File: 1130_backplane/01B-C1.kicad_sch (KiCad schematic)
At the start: 86 parts

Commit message: DN101-DN111 added to backplane schematics, DN111 01B-A1 connections made, 01B-B1 connections to be made when all signals on connectors
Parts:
- removed J431, J432, J433, J434, J435, J436, J437, J438, J439, J440, J441, J442, J443, J444, J445, J446, J447, J448, J449, J450, J451, J452, J453, J454, J455, J456, J457, J458, J459, J460, J461, J462, J463, J464, J465, J466, J467, J468, J469, J470, J471, J472, J473, J474, J475, J476, J477, J478, J479, J480, J481, J482, J483, J484, J485, J486, J487, J488, J489, J490, J491, J492, J493, J494, J495, J496, J497, J498, J499, J500, J501, J502, J503, J504, J505, J506, J507, J508, J509, J510, J511, J512, J513, J514, J515, J516: ~, symbol Connector_Generic:Conn_02x12_Row_Letter_First
- added J? (x86): ~, symbol Connector_Generic:Conn_02x12_Row_Letter_First
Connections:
- net +3V: now also J?.b2 (Pin_b2), J?.b2 (Pin_b2), J?.b2 (Pin_b2), J?.b2 (Pin_b2), J?.b2 (Pin_b2), J?.b2 (Pin_b2), J?.b2 (Pin_b2), J?.b2 (Pin_b2), J?.b2 (Pin_b2), J?.b2 (Pin_b2), J?.b2 (Pin_b2), J?.b2 (Pin_b2), J?.b2 (Pin_b2), J?.b2 (Pin_b2), J?.b2 (Pin_b2), J?.b2 (Pin_b2), J?.b2 (Pin_b2), J?.b2 (Pin_b2), J?.b2 (Pin_b2), J?.b2 (Pin_b2), J?.b2 (Pin_b2), J?.b2 (Pin_b2), J?.b2 (Pin_b2), J?.b2 (Pin_b2), J?.b2 (Pin_b2), J?.b2 (Pin_b2), J?.b2 (Pin_b2), J?.b2 (Pin_b2), J?.b2 (Pin_b2), J?.b2 (Pin_b2), J?.b2 (Pin_b2), J?.b2 (Pin_b2), J?.b2 (Pin_b2), J?.b2 (Pin_b2), J?.b2 (Pin_b2), J?.b2 (Pin_b2), J?.b2 (Pin_b2), J?.b2 (Pin_b2), J?.b2 (Pin_b2), J?.b2 (Pin_b2), J?.b2 (Pin_b2), J?.b2 (Pin_b2), J?.b2 (Pin_b2), J?.b2 (Pin_b2), J?.b2 (Pin_b2), J?.b2 (Pin_b2), J?.b2 (Pin_b2), J?.b2 (Pin_b2), J?.b2 (Pin_b2), J?.b2 (Pin_b2), J?.b2 (Pin_b2), J?.b2 (Pin_b2), J?.b2 (Pin_b2), J?.b2 (Pin_b2), J?.b2 (Pin_b2), J?.b2 (Pin_b2), J?.b2 (Pin_b2), J?.b2 (Pin_b2), J?.b2 (Pin_b2), J?.b2 (Pin_b2), J?.b2 (Pin_b2), J?.b2 (Pin_b2), J?.b2 (Pin_b2), J?.b2 (Pin_b2), J?.b2 (Pin_b2), J?.b2 (Pin_b2), J?.b2 (Pin_b2), J?.b2 (Pin_b2), J?.b2 (Pin_b2), J?.b2 (Pin_b2), J?.b2 (Pin_b2), J?.b2 (Pin_b2), J?.b2 (Pin_b2), J?.b2 (Pin_b2), J?.b2 (Pin_b2), J?.b2 (Pin_b2), J?.b2 (Pin_b2), J?.b2 (Pin_b2)
- net +6V: now also J?.a10 (Pin_a10), J?.a10 (Pin_a10), J?.a10 (Pin_a10), J?.a10 (Pin_a10), J?.a10 (Pin_a10), J?.a10 (Pin_a10), J?.a10 (Pin_a10), J?.a10 (Pin_a10), J?.a10 (Pin_a10), J?.a10 (Pin_a10), J?.a10 (Pin_a10), J?.a10 (Pin_a10), J?.a10 (Pin_a10), J?.a10 (Pin_a10), J?.a10 (Pin_a10), J?.a10 (Pin_a10), J?.a10 (Pin_a10), J?.a10 (Pin_a10), J?.a10 (Pin_a10), J?.a10 (Pin_a10), J?.a10 (Pin_a10), J?.a10 (Pin_a10), J?.a10 (Pin_a10), J?.a10 (Pin_a10), J?.a10 (Pin_a10), J?.a10 (Pin_a10), J?.a10 (Pin_a10), J?.a10 (Pin_a10), J?.a10 (Pin_a10), J?.a10 (Pin_a10), J?.a10 (Pin_a10), J?.a10 (Pin_a10), J?.a10 (Pin_a10), J?.a10 (Pin_a10), J?.a10 (Pin_a10), J?.a10 (Pin_a10), J?.a10 (Pin_a10), J?.a10 (Pin_a10), J?.a10 (Pin_a10), J?.a10 (Pin_a10), J?.a10 (Pin_a10), J?.a10 (Pin_a10), J?.a10 (Pin_a10), J?.a10 (Pin_a10), J?.a10 (Pin_a10), J?.a10 (Pin_a10), J?.a10 (Pin_a10), J?.a10 (Pin_a10), J?.a10 (Pin_a10), J?.a10 (Pin_a10), J?.a10 (Pin_a10), J?.a10 (Pin_a10), J?.a10 (Pin_a10), J?.a10 (Pin_a10), J?.a10 (Pin_a10), J?.a10 (Pin_a10), J?.a10 (Pin_a10), J?.a10 (Pin_a10), J?.a10 (Pin_a10), J?.a10 (Pin_a10), J?.a10 (Pin_a10), J?.a10 (Pin_a10), J?.a10 (Pin_a10), J?.a10 (Pin_a10), J?.a10 (Pin_a10), J?.a10 (Pin_a10), J?.a10 (Pin_a10), J?.a10 (Pin_a10), J?.a10 (Pin_a10), J?.a10 (Pin_a10), J?.a10 (Pin_a10), J?.a10 (Pin_a10), J?.a10 (Pin_a10), J?.a10 (Pin_a10), J?.a10 (Pin_a10), J?.a10 (Pin_a10), J?.a10 (Pin_a10), J?.a10 (Pin_a10)
- net -3V: now also J?.a5 (Pin_a5), J?.a5 (Pin_a5), J?.a5 (Pin_a5), J?.a5 (Pin_a5), J?.a5 (Pin_a5), J?.a5 (Pin_a5), J?.a5 (Pin_a5), J?.a5 (Pin_a5), J?.a5 (Pin_a5), J?.a5 (Pin_a5), J?.a5 (Pin_a5), J?.a5 (Pin_a5), J?.a5 (Pin_a5), J?.a5 (Pin_a5), J?.a5 (Pin_a5), J?.a5 (Pin_a5), J?.a5 (Pin_a5), J?.a5 (Pin_a5), J?.a5 (Pin_a5), J?.a5 (Pin_a5), J?.a5 (Pin_a5), J?.a5 (Pin_a5), J?.a5 (Pin_a5), J?.a5 (Pin_a5), J?.a5 (Pin_a5), J?.a5 (Pin_a5), J?.a5 (Pin_a5), J?.a5 (Pin_a5), J?.a5 (Pin_a5), J?.a5 (Pin_a5), J?.a5 (Pin_a5), J?.a5 (Pin_a5), J?.a5 (Pin_a5), J?.a5 (Pin_a5), J?.a5 (Pin_a5), J?.a5 (Pin_a5), J?.a5 (Pin_a5), J?.a5 (Pin_a5), J?.a5 (Pin_a5), J?.a5 (Pin_a5), J?.a5 (Pin_a5), J?.a5 (Pin_a5), J?.a5 (Pin_a5), J?.a5 (Pin_a5), J?.a5 (Pin_a5), J?.a5 (Pin_a5), J?.a5 (Pin_a5), J?.a5 (Pin_a5), J?.a5 (Pin_a5), J?.a5 (Pin_a5), J?.a5 (Pin_a5), J?.a5 (Pin_a5), J?.a5 (Pin_a5), J?.a5 (Pin_a5), J?.a5 (Pin_a5), J?.a5 (Pin_a5), J?.a5 (Pin_a5), J?.a5 (Pin_a5), J?.a5 (Pin_a5), J?.a5 (Pin_a5), J?.a5 (Pin_a5), J?.a5 (Pin_a5), J?.a5 (Pin_a5), J?.a5 (Pin_a5), J?.a5 (Pin_a5), J?.a5 (Pin_a5), J?.a5 (Pin_a5), J?.a5 (Pin_a5), J?.a5 (Pin_a5), J?.a5 (Pin_a5), J?.a5 (Pin_a5), J?.a5 (Pin_a5), J?.a5 (Pin_a5), J?.a5 (Pin_a5), J?.a5 (Pin_a5), J?.a5 (Pin_a5), J?.a5 (Pin_a5), J?.a5 (Pin_a5)
- net GND: now also J?.b7 (Pin_b7), J?.b7 (Pin_b7), J?.b7 (Pin_b7), J?.b7 (Pin_b7), J?.b7 (Pin_b7), J?.b7 (Pin_b7), J?.b7 (Pin_b7), J?.b7 (Pin_b7), J?.b7 (Pin_b7), J?.b7 (Pin_b7), J?.b7 (Pin_b7), J?.b7 (Pin_b7), J?.b7 (Pin_b7), J?.b7 (Pin_b7), J?.b7 (Pin_b7), J?.b7 (Pin_b7), J?.b7 (Pin_b7), J?.b7 (Pin_b7), J?.b7 (Pin_b7), J?.b7 (Pin_b7), J?.b7 (Pin_b7), J?.b7 (Pin_b7), J?.b7 (Pin_b7), J?.b7 (Pin_b7), J?.b7 (Pin_b7), J?.b7 (Pin_b7), J?.b7 (Pin_b7), J?.b7 (Pin_b7), J?.b7 (Pin_b7), J?.b7 (Pin_b7), J?.b7 (Pin_b7), J?.b7 (Pin_b7), J?.b7 (Pin_b7), J?.b7 (Pin_b7), J?.b7 (Pin_b7), J?.b7 (Pin_b7), J?.b7 (Pin_b7), J?.b7 (Pin_b7), J?.b7 (Pin_b7), J?.b7 (Pin_b7), J?.b7 (Pin_b7), J?.b7 (Pin_b7), J?.b7 (Pin_b7), J?.b7 (Pin_b7), J?.b7 (Pin_b7), J?.b7 (Pin_b7), J?.b7 (Pin_b7), J?.b7 (Pin_b7), J?.b7 (Pin_b7), J?.b7 (Pin_b7), J?.b7 (Pin_b7), J?.b7 (Pin_b7), J?.b7 (Pin_b7), J?.b7 (Pin_b7), J?.b7 (Pin_b7), J?.b7 (Pin_b7), J?.b7 (Pin_b7), J?.b7 (Pin_b7), J?.b7 (Pin_b7), J?.b7 (Pin_b7), J?.b7 (Pin_b7), J?.b7 (Pin_b7), J?.b7 (Pin_b7), J?.b7 (Pin_b7), J?.b7 (Pin_b7), J?.b7 (Pin_b7), J?.b7 (Pin_b7), J?.b7 (Pin_b7), J?.b7 (Pin_b7), J?.b7 (Pin_b7), J?.b7 (Pin_b7), J?.b7 (Pin_b7), J?.b7 (Pin_b7), J?.b7 (Pin_b7), J?.b7 (Pin_b7), J?.b7 (Pin_b7), J?.b7 (Pin_b7), J?.b7 (Pin_b7), J?.b7 (Pin_b7), J?.b7 (Pin_b7), J?.b7 (Pin_b7), J?.b7 (Pin_b7), J?.b7 (Pin_b7), J?.b7 (Pin_b7), J?.b7 (Pin_b7), J?.b7 (Pin_b7)

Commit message: Add labels for bottom T[x] connectors, finished page DU101.
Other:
- moved on the sheet: J?

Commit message: Redo annotations...
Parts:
- gave numbers to parts that had none: 86

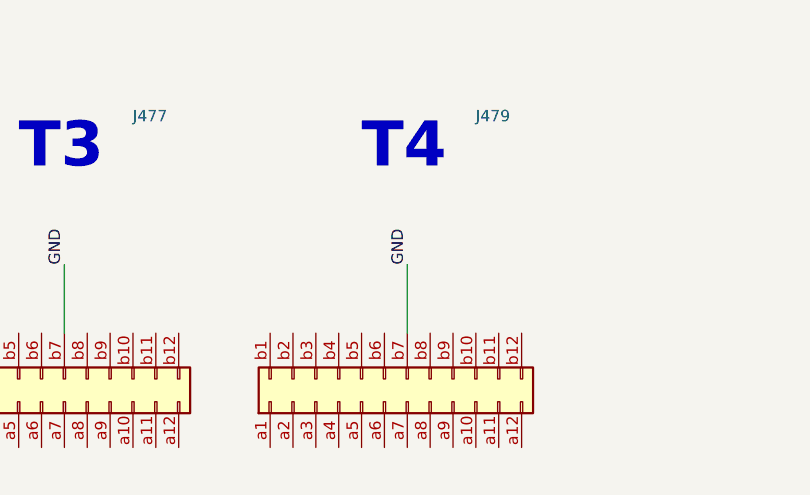
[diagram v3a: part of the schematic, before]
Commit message: Finish page KR101-KR111
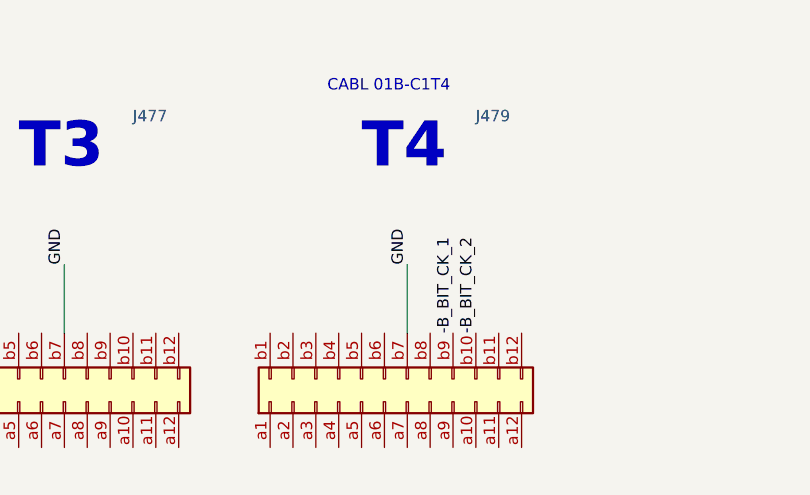
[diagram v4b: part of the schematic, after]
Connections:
- net -B_BIT_CK_2: now reaches J479.b10 (Pin_b10)
- net -B_BIT_CK_1: now reaches J479.b9 (Pin_b9)
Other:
- note added: "CABL 01B-C1T4"
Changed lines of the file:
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@@
     (effects (font (size 5 5) (thickness 1) bold) (justify left bottom))
+  )
+  (text "CABL 01B-C1T4" (at 469.9 24.13 0)
+    (effects (font (size 1.27 1.27)) (justify left bottom))
   )
   (text "C" (at 163.83 337.82 0)
@@
     (effects (font (size 1.27 1.27)) (justify right bottom))
   )
+  (label "-B_BIT_CK_1" (at 483.87 50.8 90)
+    (effects (font (size 1.27 1.27)) (justify left bottom))
+  )
   (label "-3V" (at 469.9 266.7 180)
     (effects (font (size 1.27 1.27)) (justify right bottom))
@@
     (effects (font (size 1.27 1.27)) (justify left bottom))
   )
+  (label "-B_BIT_CK_2" (at 486.41 50.8 90)
+    (effects (font (size 1.27 1.27)) (justify left bottom))
+  )

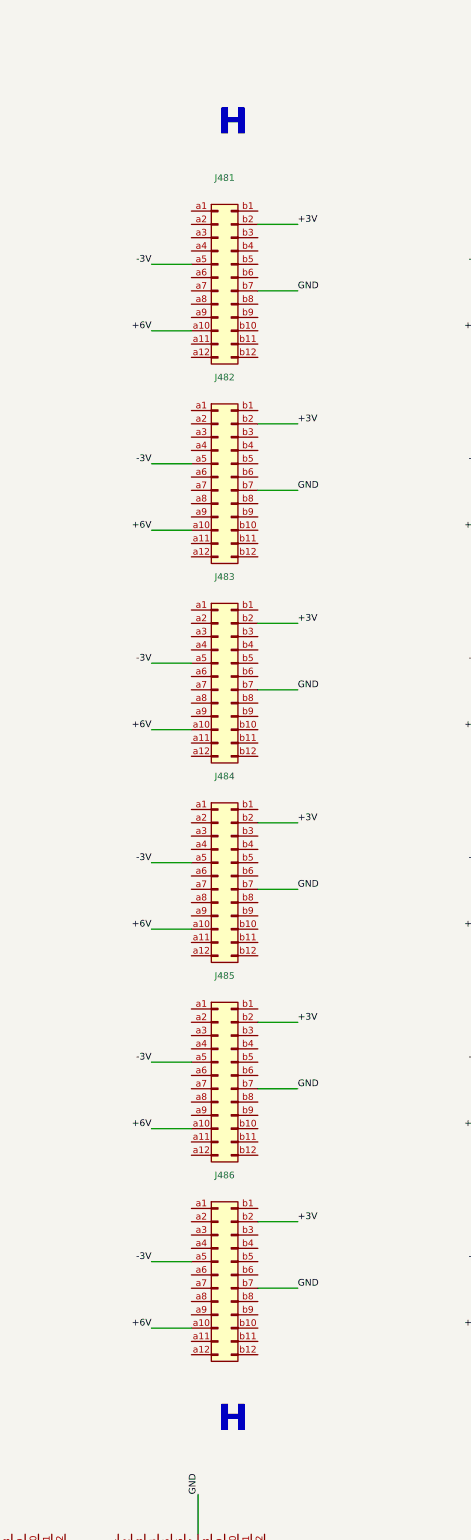
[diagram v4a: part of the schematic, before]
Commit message: Finish page KU301-KU311, minor column label fix.
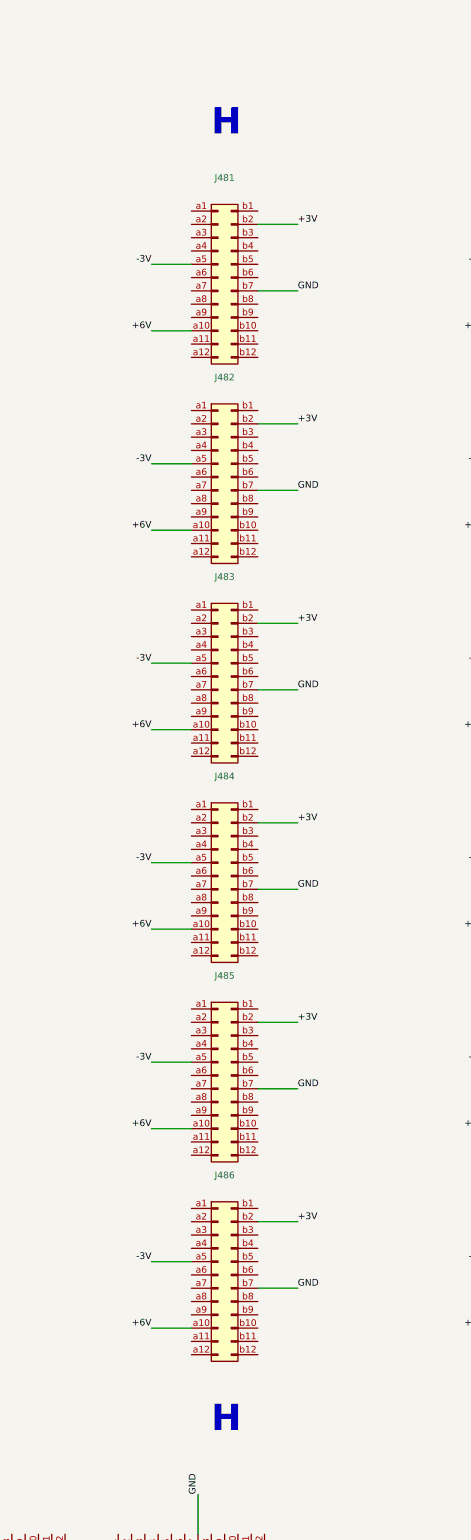
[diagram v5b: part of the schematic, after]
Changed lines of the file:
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@@
     (effects (font (size 5 5) (thickness 1) bold) (justify left bottom))
   )
-  (text "H" (at 482.6 337.82 0)
+  (text "H" (at 481.33 337.82 0)
     (effects (font (size 5 5) (thickness 1) bold) (justify left bottom))
   )
@@
     (effects (font (size 1.27 1.27)) (justify left bottom))
   )
-  (text "H" (at 482.6 90.17 0)
+  (text "H" (at 481.33 90.17 0)
     (effects (font (size 5 5) (thickness 1) bold) (justify left bottom))
   )

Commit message: Actually finish MB101...
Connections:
- net -STORAGE_ADDRESS_10: now reaches J477.a10 (Pin_a10)
- net -STORAGE_ADDRESS_10: now also J477.a7 (Pin_a7)
- net -STORAGE_ADDRESS_12: now reaches J477.a11 (Pin_a11)
- net -STORAGE_ADDRESS_14: now reaches J477.a12 (Pin_a12)
- net -STORAGE_ADDRESS_4: now reaches J477.a3 (Pin_a3)
- net -STORAGE_ADDRESS_6: now reaches J477.a4 (Pin_a4)
- net -STORAGE_ADDRESS_8: now reaches J477.a9 (Pin_a9)
- net -STORAGE_ADDRESS_11: now reaches J477.b10 (Pin_b10)
- net -STORAGE_ADDRESS_13: now reaches J477.b11 (Pin_b11)
- net -STORAGE_ADDRESS_15: now reaches J477.b12 (Pin_b12)
- net -STORAGE_ADDRESS_3: now reaches J477.b2 (Pin_b2)
- net -STORAGE_ADDRESS_5: now reaches J477.b3 (Pin_b3)
- net -STORAGE_ADDRESS_7: now reaches J477.b4 (Pin_b4)
- net -STORAGE_ADDRESS_9: now reaches J477.b9 (Pin_b9)
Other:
- note added: "CABL 01B-B1T3"
- note added: "CABL 01B-B1T4"
- note removed: "CABL 01B-C1T4"
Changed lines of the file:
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@@
     (effects (font (size 5 5) (thickness 1) bold) (justify left bottom))
   )
-  (text "CABL 01B-C1T4" (at 469.9 24.13 0)
+  (text "CABL 01B-B1T4" (at 469.9 24.13 0)
     (effects (font (size 1.27 1.27)) (justify left bottom))
   )
@@
     (effects (font (size 1.27 1.27)) (justify left bottom))
   )
+  (text "CABL 01B-B1T3" (at 431.8 24.13 0)
+    (effects (font (size 1.27 1.27)) (justify left bottom))
+  )
   (text "A" (at 29.21 38.1 0)
     (effects (font (size 5 5) (thickness 1) bold) (justify left bottom))
@@
     (effects (font (size 1.27 1.27)) (justify left bottom))
   )
+  (label "-STORAGE_ADDRESS_3" (at 427.99 50.8 90)
+    (effects (font (size 1.27 1.27)) (justify left bottom))
+  )
   (label "+3V" (at 497.84 259.08 0)
     (effects (font (size 1.27 1.27)) (justify left bottom))
@@
     (effects (font (size 1.27 1.27)) (justify right bottom))
   )
+  (label "-STORAGE_ADDRESS_13" (at 450.85 50.8 90)
+    (effects (font (size 1.27 1.27)) (justify left bottom))
+  )
   (label "GND" (at 116.84 233.68 0)
     (effects (font (size 1.27 1.27)) (justify left bottom))
@@
     (effects (font (size 1.27 1.27)) (justify right bottom))
   )
+  (label "-STORAGE_ADDRESS_9" (at 445.77 50.8 90)
+    (effects (font (size 1.27 1.27)) (justify left bottom))
+  )
   (label "GND" (at 624.84 119.38 0)
     (effects (font (size 1.27 1.27)) (justify left bottom))
@@
     (effects (font (size 1.27 1.27)) (justify left bottom))
   )
+  (label "-STORAGE_ADDRESS_11" (at 448.31 50.8 90)
+    (effects (font (size 1.27 1.27)) (justify left bottom))
+  )
   (label "GND" (at 624.84 309.88 0)
     (effects (font (size 1.27 1.27)) (justify left bottom))
@@
     (effects (font (size 1.27 1.27)) (justify left bottom))
   )
+  (label "-STORAGE_ADDRESS_6" (at 433.07 63.5 270)
+    (effects (font (size 1.27 1.27)) (justify right bottom))
+  )
   (label "+6V" (at 152.4 165.1 180)
     (effects (font (size 1.27 1.27)) (justify right bottom))
@@
     (effects (font (size 1.27 1.27)) (justify right bottom))
   )
+  (label "-STORAGE_ADDRESS_4" (at 430.53 63.5 270)
+    (effects (font (size 1.27 1.27)) (justify right bottom))
+  )
   (label "-3V" (at 25.4 304.8 180)
     (effects (font (size 1.27 1.27)) (justify right bottom))
@@
     (effects (font (size 1.27 1.27)) (justify left bottom))
   )
+  (label "-STORAGE_ADDRESS_10" (at 448.31 63.5 270)
+    (effects (font (size 1.27 1.27)) (justify right bottom))
+  )
   (label "GND" (at 497.84 119.38 0)
     (effects (font (size 1.27 1.27)) (justify left bottom))
@@
     (effects (font (size 1.27 1.27)) (justify left bottom))
   )
+  (label "-STORAGE_ADDRESS_10" (at 440.69 63.5 270)
+    (effects (font (size 1.27 1.27)) (justify right bottom))
+  )
   (label "-3V" (at 406.4 152.4 180)
     (effects (font (size 1.27 1.27)) (justify right bottom))
@@
     (effects (font (size 1.27 1.27)) (justify right bottom))
   )
+  (label "-STORAGE_ADDRESS_14" (at 453.39 63.5 270)
+    (effects (font (size 1.27 1.27)) (justify right bottom))
+  )
   (label "+3V" (at 624.84 182.88 0)
     (effects (font (size 1.27 1.27)) (justify left bottom))
@@
     (effects (font (size 1.27 1.27)) (justify right bottom))
   )
+  (label "-STORAGE_ADDRESS_7" (at 433.07 50.8 90)
+    (effects (font (size 1.27 1.27)) (justify left bottom))
+  )
   (label "GND" (at 243.84 195.58 0)
     (effects (font (size 1.27 1.27)) (justify left bottom))
@@
     (effects (font (size 1.27 1.27)) (justify left bottom))
   )
+  (label "-STORAGE_ADDRESS_15" (at 453.39 50.8 90)
+    (effects (font (size 1.27 1.27)) (justify left bottom))
+  )
   (label "+3V" (at 561.34 259.08 0)
     (effects (font (size 1.27 1.27)) (justify left bottom))
@@
     (effects (font (size 1.27 1.27)) (justify right bottom))
   )
+  (label "-STORAGE_ADDRESS_5" (at 430.53 50.8 90)
+    (effects (font (size 1.27 1.27)) (justify left bottom))
+  )
   (label "+6V" (at 25.4 279.4 180)
     (effects (font (size 1.27 1.27)) (justify right bottom))
@@
     (effects (font (size 1.27 1.27)) (justify left bottom))
   )
+  (label "-STORAGE_ADDRESS_12" (at 450.85 63.5 270)
+    (effects (font (size 1.27 1.27)) (justify right bottom))
+  )
   (label "GND" (at 624.84 157.48 0)
     (effects (font (size 1.27 1.27)) (justify left bottom))
@@
     (effects (font (size 1.27 1.27)) (justify left bottom))
   )
+  (label "-STORAGE_ADDRESS_8" (at 445.77 63.5 270)
+    (effects (font (size 1.27 1.27)) (justify right bottom))
+  )
   (label "+6V" (at 406.4 127 180)

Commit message: Finish page MC101
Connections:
- net +STORAGE_WRITE_CYCLE: now reaches J477.a1 (Pin_a1)
- net +STORAGE_WRITE_CYCLE: now also J477.a5 (Pin_a5)
- net +STORAGE_READ_CYCLE: now reaches J477.a6 (Pin_a6)
- net +STORAGE_USE: now reaches J477.a8 (Pin_a8)
- net +STORAGE_SELECT: now reaches J477.b8 (Pin_b8)
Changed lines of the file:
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@@
+    (effects (font (size 1.27 1.27)) (justify right bottom))
+  )
+  (label "+STORAGE_USE" (at 443.23 63.5 270)
     (effects (font (size 1.27 1.27)) (justify right bottom))
   )
@@
     (effects (font (size 1.27 1.27)) (justify left bottom))
   )
+  (label "+STORAGE_WRITE_CYCLE" (at 435.61 63.5 270)
+    (effects (font (size 1.27 1.27)) (justify right bottom))
+  )
   (label "+3V" (at 561.34 220.98 0)
     (effects (font (size 1.27 1.27)) (justify left bottom))
@@
     (effects (font (size 1.27 1.27)) (justify left bottom))
   )
+  (label "+STORAGE_READ_CYCLE" (at 438.15 63.5 270)
+    (effects (font (size 1.27 1.27)) (justify right bottom))
+  )
   (label "+6V" (at 533.4 165.1 180)
     (effects (font (size 1.27 1.27)) (justify right bottom))
@@
     (effects (font (size 1.27 1.27)) (justify right bottom))
   )
+  (label "+STORAGE_WRITE_CYCLE" (at 425.45 63.5 270)
+    (effects (font (size 1.27 1.27)) (justify right bottom))
+  )
   (label "-STORAGE_ADDRESS_5" (at 430.53 50.8 90)
     (effects (font (size 1.27 1.27)) (justify left bottom))
@@
     (effects (font (size 1.27 1.27)) (justify left bottom))
   )
+  (label "+STORAGE_SELECT" (at 443.23 50.8 90)
+    (effects (font (size 1.27 1.27)) (justify left bottom))
+  )
